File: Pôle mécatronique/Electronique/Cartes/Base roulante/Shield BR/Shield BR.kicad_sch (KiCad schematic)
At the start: 21 parts, among them J0 Conn_01x04_Female, J1 Conn_01x04_Female, J2 Conn_01x04_Female, J3 Conn_01x04_Female, J4 Conn_01x02_Male, SW1 SW_DIP_x04, SW2 SW_Push_SPDT, U4 R-78E5.0-0.5

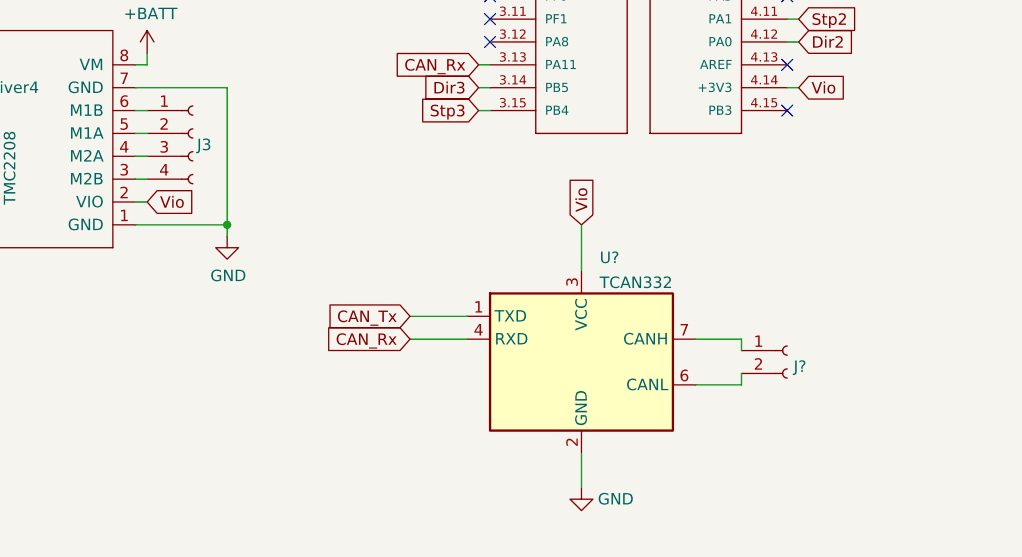
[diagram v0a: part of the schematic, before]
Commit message: Update BR et alim
- Mise à jour BR pour 2022 (taille de piste, modèle 3D ...)

- Changements mineurs sur l'alim
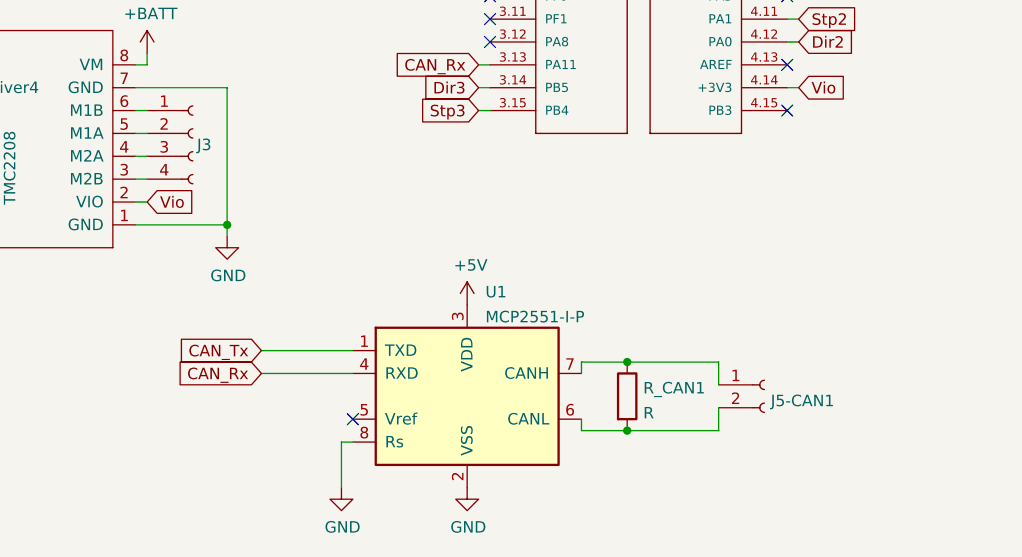
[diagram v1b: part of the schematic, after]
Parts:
- removed J?: Conn_01x02_Female, Connector_JST:JST_PH_B2B-PH-K_1x02_P2.00mm_Vertical, symbol Connector:Conn_01x02_Female
- removed U?: TCAN332, symbol Interface_CAN_LIN:TCAN332
- added J5-CAN1: Conn_01x02_Female, Connector_JST:JST_PH_B2B-PH-K_1x02_P2.00mm_Vertical, symbol Connector:Conn_01x02_Female
- added R_CAN1: R, Resistor_THT:R_Axial_DIN0207_L6.3mm_D2.5mm_P7.62mm_Horizontal, symbol Device:R
- added U1: MCP2551-I-P, Package_DIP:DIP-8_W7.62mm, symbol Interface_CAN_LIN:MCP2551-I-P
- Driver1, Driver2, Driver3, Driver4: footprint Trinamic_Drivers:TMC_2208_BOB -> Autre:MODULE_TMC2208_SILENTSTEPSTICK; symbol Trinamic_Drivers:TMC2208 -> Shield-BR-rescue:TMC2208-Trinamic_Drivers
- J4: value Conn_01x02_Male -> Conn_01x04_Male
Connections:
- net +5V: now also U1.3 (VDD)
- net CAN_Rx: now also U1.4 (RXD)
- net CAN_Tx: now also U1.1 (TXD)
- net GND: now also U1.2 (VSS), U1.8 (Rs)
- new net: J5-CAN1.1 (Pin_1), R_CAN1.1, U1.7 (CANH)
- new net: J5-CAN1.2 (Pin_2), R_CAN1.2, U1.6 (CANL)
- no-connect marks 26 -> 27

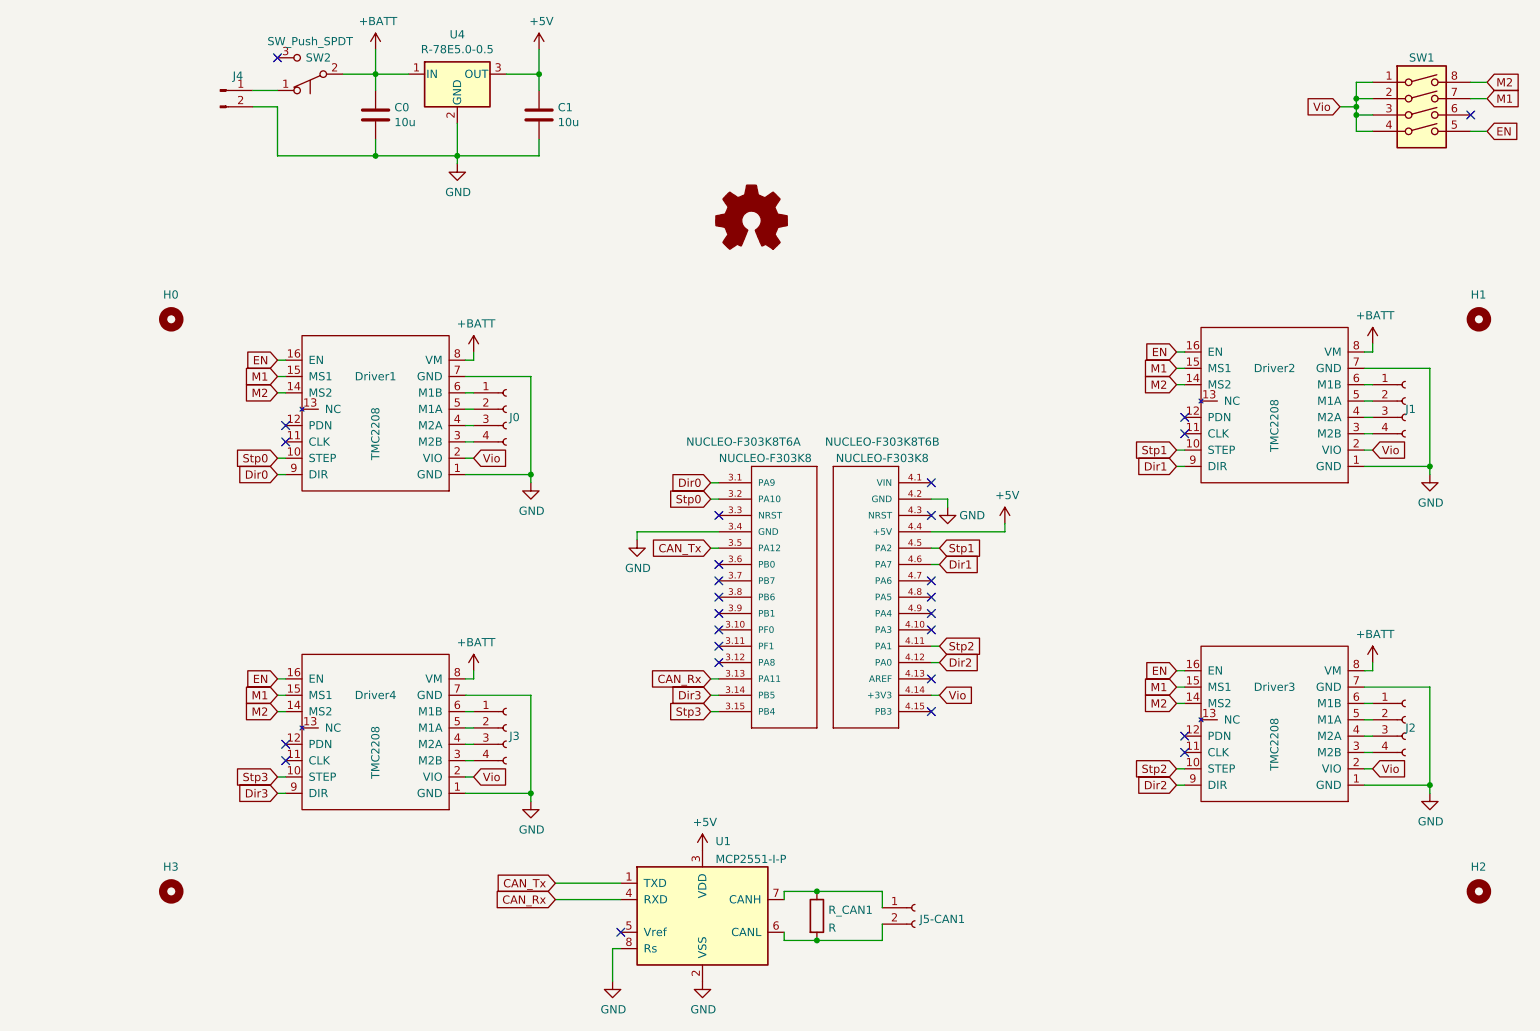
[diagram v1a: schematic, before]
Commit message: Update BR
- Avancement raccords EN/MS1/MS2
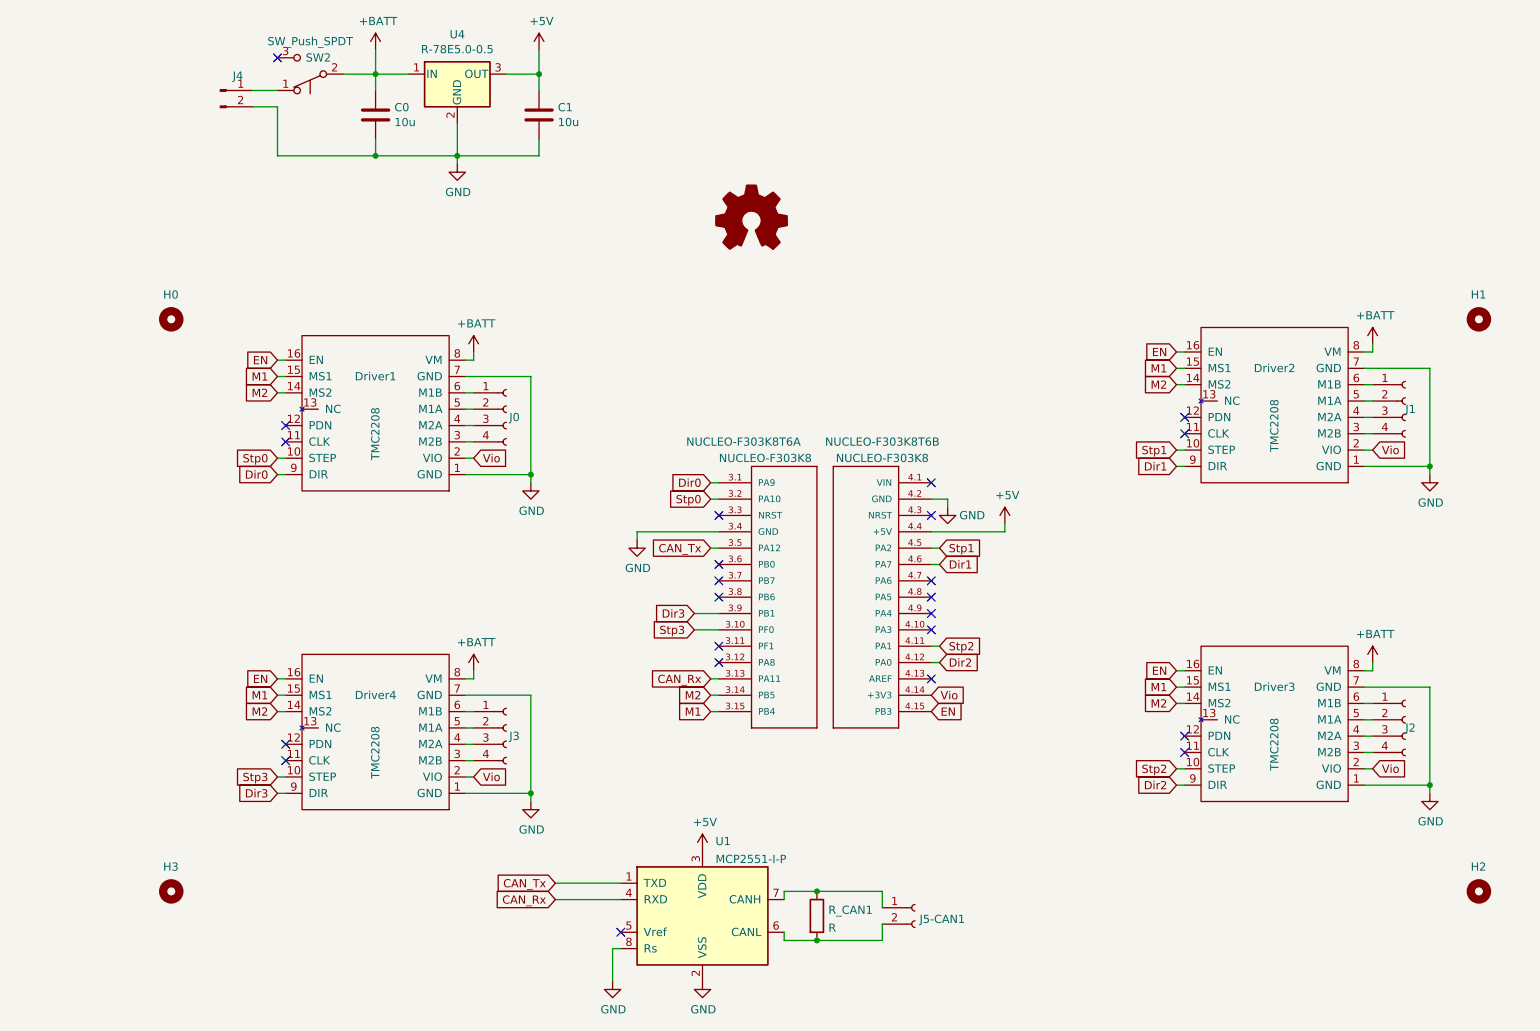
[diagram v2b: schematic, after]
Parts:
- removed SW1: SW_DIP_x04, Button_Switch_THT:SW_DIP_SPSTx04_Slide_9.78x12.34mm_W7.62mm_P2.54mm, symbol Switch:SW_DIP_x04
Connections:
- net Dir3: now also NUCLEO-F303K8T6.3.9 (PB1); no longer NUCLEO-F303K8T6.3.14 (PB5)
- net EN: now also NUCLEO-F303K8T6.4.15 (PB3)
- net M1: now also NUCLEO-F303K8T6.3.15 (PB4)
- net M2: now also NUCLEO-F303K8T6.3.14 (PB5)
- net Stp3: now also NUCLEO-F303K8T6.3.10 (PF0); no longer NUCLEO-F303K8T6.3.15 (PB4)
- no-connect marks 27 -> 23

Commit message: Update BR
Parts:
- added C1: 100nF, Capacitor_SMD:C_1206_3216Metric_Pad1.33x1.80mm_HandSolder, symbol Device:C
- added C2: 100pF, Capacitor_SMD:C_1206_3216Metric_Pad1.33x1.80mm_HandSolder, symbol Device:C
- added C5: 100n, Capacitor_SMD:C_1206_3216Metric_Pad1.33x1.80mm_HandSolder, symbol Device:C
- added C6, C7, C8, C9: 220 à 1000 µF, Capacitor_SMD:C_Elec_8x10.2, symbol Device:C_Polarized
- added TP1, TP2, TP3, TP4, TP5, TP6, TP7, TP8, TP9: TestPoint, TestPoint:TestPoint_Pad_D2.0mm, symbol Connector:TestPoint
- C3: renamed from C0; footprint Capacitor_SMD:C_1206_3216Metric_Pad1.42x1.75mm_HandSolder -> Capacitor_SMD:C_1206_3216Metric_Pad1.33x1.80mm_HandSolder
- C4: renamed from C1; footprint Capacitor_SMD:C_1206_3216Metric_Pad1.42x1.75mm_HandSolder -> Capacitor_SMD:C_1206_3216Metric_Pad1.33x1.80mm_HandSolder
- renumbered Driver4 to Driver3, Driver3 to Driver4, H0 to H2, H2 to H4, J4 to J1, J0 to J2, J1 to J3, J3 to J4, J2 to J5, NUCLEO-F303K8T6 to NUCLEO-F303K8T1, SW2 to SW1, U4 to U1, U1 to U2
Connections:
- net +5V: now also C1.1, C2.1, C5.1, TP1.1
- net +BATT: now also C6.1, C7.1, C8.1, C9.1, TP2.1
- net CAN_Rx: now also TP6.1
- net CAN_Tx: now also TP5.1
- net EN: now also TP9.1
- net GND: now also C1.2, C2.2, C5.2, C6.2, C7.2, C8.2, C9.2
- net M1: now also TP8.1
- net M2: now also TP7.1
- net at J5-CAN1.1 (Pin_1), R_CAN1.1, U2.7 (CANH): now also TP3.1
- net at J5-CAN1.2 (Pin_2), R_CAN1.2, U2.6 (CANL): now also TP4.1
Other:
- moved on the sheet: C3, C4, Driver1, Driver2, Driver3, H1, J1, J2, J3, J4, J5-CAN1, NUCLEO-F303K8T1A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
